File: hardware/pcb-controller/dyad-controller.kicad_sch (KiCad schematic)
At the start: 36 parts, among them J1 USB_C_Receptacle_USB2.0, J2 SWD, J6 HC-FPC-0.5-20P-FH20, J7 HC-FPC-0.5-20P-FH20, J8 HC-FPC-0.5-14P-FH20, SW1 SW_Push, U1 W25Q128JVS, U2 USBLC6-2SC6, U3 RP2040, U4 XC6206PxxxMR-Regulator_Linear, Y1 12MHz

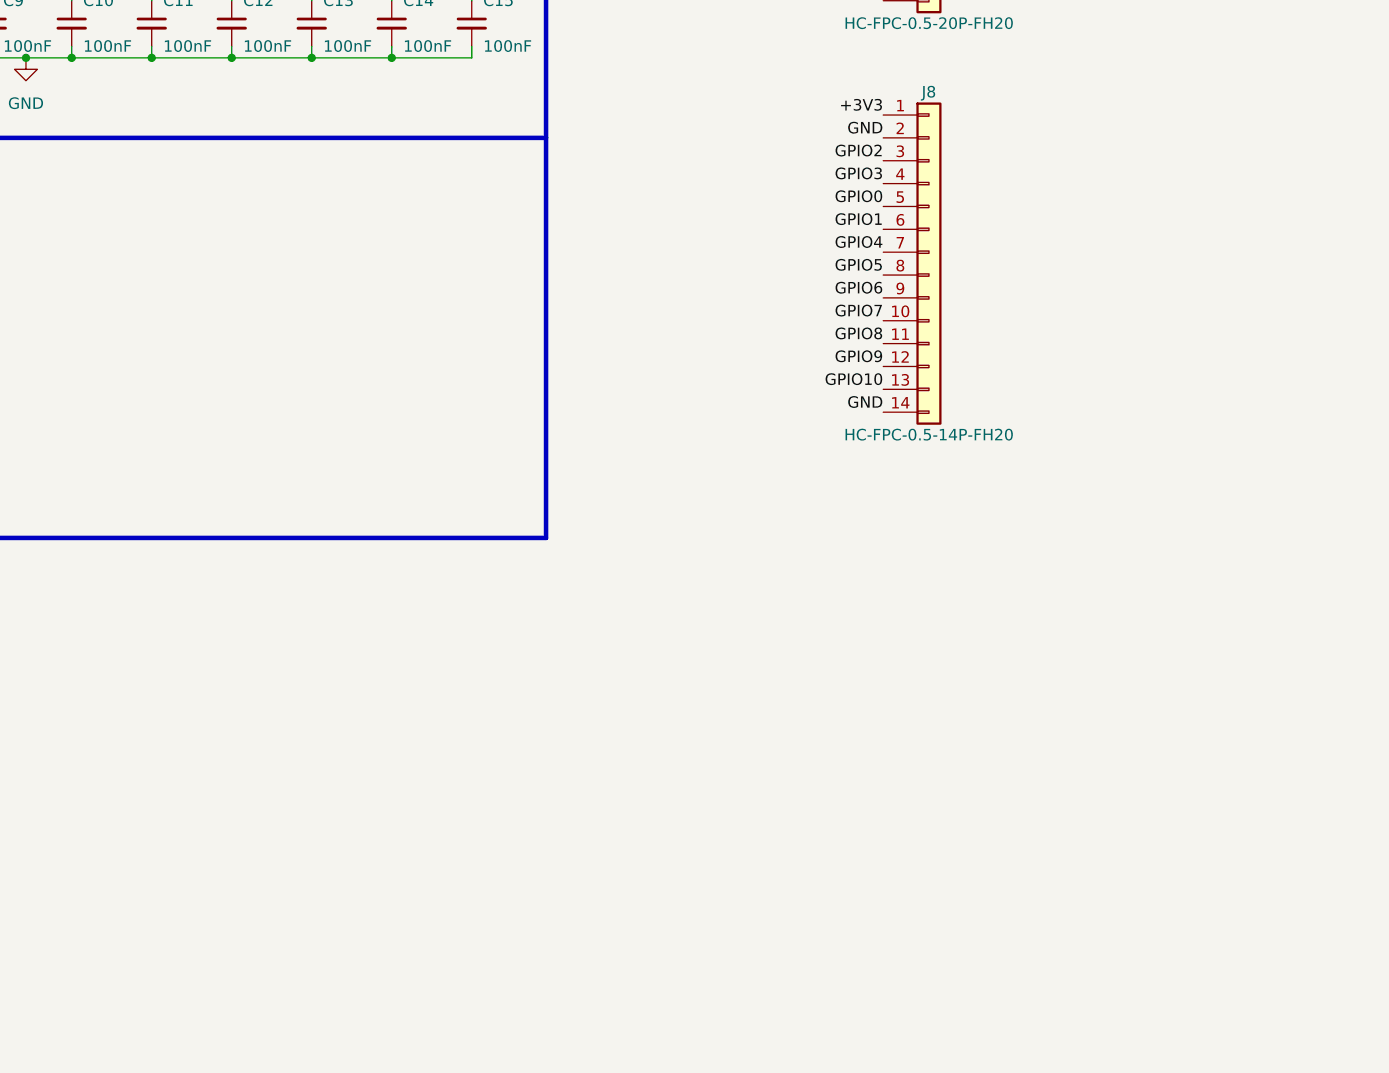
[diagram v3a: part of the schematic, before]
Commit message: Add the split-link USB-C, duplicated on both side edges
J9 and J10, same receptacle and footprint as the host J1 per PLAN.md §5,
one populated per half -- whichever faces the other half.

The host port stays a single footprint on the rear edge. The single
controller orientation the two-FFC decision buys means a rear-edge port
lands identically in both halves, so the host needs no duplicating. The
split port is duplicated for **usability, not geometry**: PLAN.md §5 warns
that "two identical USB-C ports per half invite the wrong cable.
Distinguish them by case position and labelling." Two ports side by side on
the rear are not distinguishable by position, and on the slave half there is
no host cable plugged in to compare against. On the inboard edge the split
port is structurally unmistakable -- the cable to the other half leaves from
the side facing it.

Wired to the three safety rules, not around them:

  CC1/CC2 no-connect (rule 1) -- a compliant source enables no VBUS without
  an Rd, so plugging the split port into a host is inert.
  SBU1 and SBU2 both tied to GPIO11 (rule 2) -- USB-C is reversible, and a
  single SBU pin would drop the link on a flipped plug.
  VBUS on its own VBUS_SPLIT rail (rule 3), awaiting its fuse and OR-ing
  Schottky, which are the next parts due.

D+/D- is deliberately left unconnected. The split link is not USB; wiring
the D pair would mean a C-to-C cable shorting the two halves' RP2040 USB
data lines with both device PHYs driving. Both D pairs carry explicit
no-connect flags, 12 in total across the two connectors.

Numbers: errors 4 -> 3. GPIO11 clears -- it was the last of the fifteen the
header deletion exposed that a connector could fix. The remaining three are
GPIO27-29, the genuine spares. 0 shorts, 0 orphans, the same 4 overlaps
inherited from the vendored design.

The three lib_symbol_issues warnings are one pre-existing issue, not two new
ones: J1 has always carried "Symbol 'USB_C_Receptacle_USB2.0' not found in
library 'Conne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
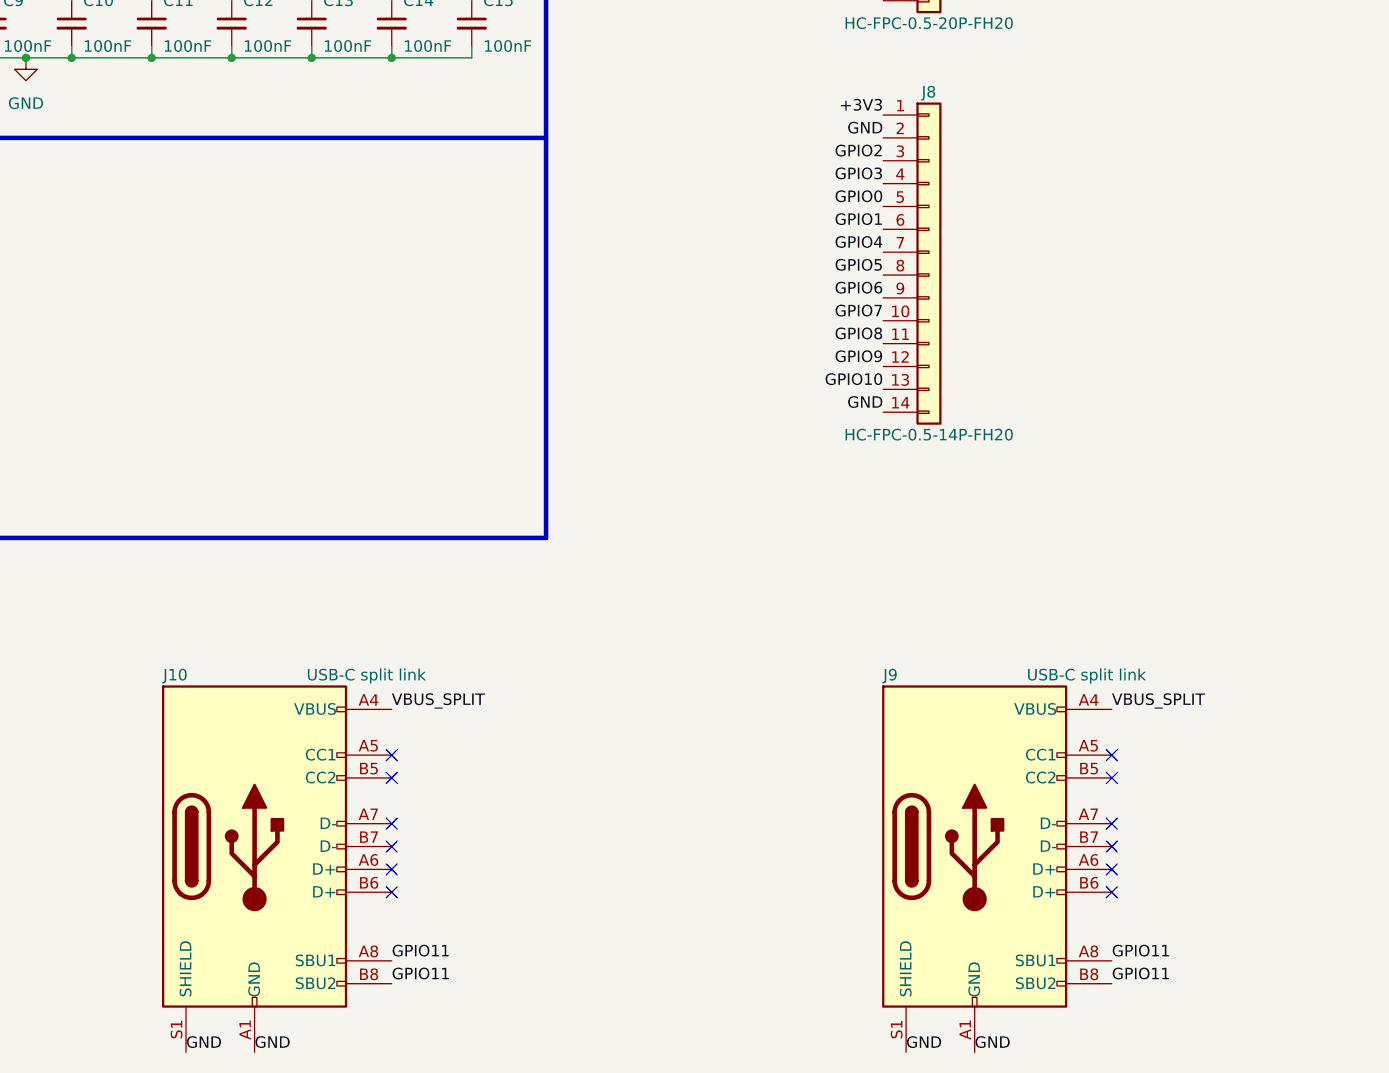
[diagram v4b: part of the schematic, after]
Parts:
- added J10, J9: USB-C split link, Connector_USB:USB_C_Receptacle_HRO_TYPE-C-31-M-12, symbol Connector:USB_C_Receptacle_USB2.0
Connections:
- net GND: now also J10.A1 (GND), J10.A12 (GND), J10.B1 (GND), J10.B12 (GND), J10.S1 (SHIELD), J9.A1 (GND), J9.A12 (GND), J9.B1 (GND), J9.B12 (GND), J9.S1 (SHIELD)
- net GPIO11: now also J10.A8 (SBU1), J10.B8 (SBU2), J9.A8 (SBU1), J9.B8 (SBU2)
- new net VBUS_SPLIT: J10.A4 (VBUS), J10.A9 (VBUS), J10.B4 (VBUS), J10.B9 (VBUS), J9.A4 (VBUS), J9.A9 (VBUS), J9.B4 (VBUS), J9.B9 (VBUS)
- no-connect marks 2 -> 14

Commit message: Add the split-VBUS fuse and the 5 V OR-ing Schottky
F2 (500 mA polyfuse, C70076, same part as F1) on the split VBUS, and D1
(SS34 Schottky, C8678, JLCPCB Basic, 3 A / 40 V) in the host VBUS path.
This completes PLAN.md §5 rule 3.

  host VBUS --F1--> VBUS_FUSED -->|D1--+--> +5V  (LDO, ESD, LED rail)
                                        |
                    split VBUS --F2-----+       (J9/J10, to the other half)

**Where the Schottky goes is not free choice** -- it decides whether one
half can power the other. +5V is the shared node: it feeds this half and
reaches the other half through F2 and the cable, while each half's own VBUS
enters through its own D1, so two hosts can never meet VBUS-to-VBUS. That is
the hazard rule 3 actually names.

The alternatives fail. A diode on each input into +5V blocks cross-half
power entirely. A diode only on the split input is worse -- a half can
receive but none can ever send. The Schottky must sit in the host path.

This required surgery on the inherited power tree: F1 pin 2 fed +5V
directly, so the wire and its +5V symbol were removed and F1's output
renamed VBUS_FUSED, with D1 bridging to +5V. Verified by reading both nets
back -- VBUS_FUSED holds exactly F1 pin 2 and D1's anode, and +5V holds D1's
cathode, F2, the LDO input, the ESD part, C16, the PWR_FLAG and J6/J7.
Polarity confirmed from the symbol: D1 pin 2 is A, pin 1 is K.

**Consequence to price in: +5V is now ~4.6 V, not 5.0 V.** SS34 drops ~0.4 V
at 1 A. Downstream still has margin -- XC6206 needs ~3.55 V in, SK6812MINI-E
is specified from 3.7 V -- but PLAN.md §5's per-key RGB brightness budget
assumes a 5 V rail and should be re-checked against 4.6 V before the LED
ceiling is treated as final. Recorded in CONTROLLER.md §2 rather than left
to be discovered.

SS34 over the 1 A B5819W (C8598, also Basic) for headroom: with one port
feeding both halves the diode carries the whole board.

Numbers: errors unchanged at 3, still only GPIO27-29, the genuine spares.
endpoin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
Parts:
- added D1: SS34, Diode_SMD:D_SMA, symbol Device:D_Schottky
- added F2: 500mA, Fuse:Fuse_1206_3216Metric, symbol Device:Polyfuse_Small
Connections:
- net +5V: now also D1.1 (K), F2.2; no longer F1.2
- net VBUS_SPLIT: now also F2.1
- new net VBUS_FUSED: D1.2 (A), F1.2
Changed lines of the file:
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@@
 	(wire
 		(pts
-			(xy 272.415 29.21)
-			(xy 277.495 29.21)
-		)
-		(stroke
-			(width 0)
-			(type default)
-		)
-	)
-	(wire
-		(pts
 			(xy 93.98 107.95)
 			(xy 88.9 107.95)
@@
 		)
 	)
+  (label "VBUS_FUSED"
+    (at 272.415 29.21 0)
+    (fields_autoplaced yes)
+    (effects (font (size 1.27 1.27)) (justify left bottom))
+  )
+  (label "VBUS_FUSED"
+    (at 144.78 175.26 0)
+    (fields_autoplaced yes)
+    (effects (font (size 1.27 1.27)) (justify left bottom))
+  )
+  (label "+5V"
+    (at 137.16 175.26 180)
+    (fields_autoplaced yes)
+    (effects (font (size 1.27 1.27)) (justify right bottom))
+  )
+  (label "+5V"
+    (at 140.97 199.39 0)
+    (fields_autoplaced yes)
+    (effects (font (size 1.27 1.27)) (justify left bottom))
+  )
+  (label "VBUS_SPLIT"
+    (at 140.97 194.31 0)
+    (fields_autoplaced yes)
+    (effects (font (size 1.27 1.27)) (justify left bottom))
+  )
 	(symbol
 		(lib_id "Device:R_Small")
@@
 	)
 	(symbol
-		(lib_id "power:+5V")
-		(at 277.495 29.21 0)
-		(unit 1)
-		(exclude_from_sim no)
-		(in_bom yes)
-		(on_board yes)
-		(dnp no)
-		(fields_autoplaced)
-		(property "Reference" "#PWR09"
-			(at 277.495 33.02 0)
-			(hide yes)
-			(show_name no)
-			(do_not_autoplace no)
-			(effects
-				(font
-					(size 1.27 1.27)
-				)
-			)
-		)
-		(property "Value" "+5V"
-			(at 277.495 24.13 0)
-			(show_name no)
-			(do_not_autoplace no)
-			(effects
-				(font
-					(size 1.27 1.27)
-				)
-			)
-		)
-		(property "Footprint" ""
-			(at 277.495 29.21 0)
-			(hide yes)
-			(show_name no)
-			(do_not_autoplace no)
-			(effects
-				(font
-					(size 1.27 1.27)
-				)
-			)
-		)
-		(property "Datasheet" ""
-			(at 277.495 29.21 0)
-			(hide yes)
-			(show_name no)
-			(do_not_autoplace no)
-			(effects
-				(font
-					(size 1.27 1.27)
-				)
-			)
-		)
-		(property "Description" ""
-			(at 277.495 29.21 0)
-			(show_name no)
-			(do_not_autoplace no)
-			(effects
-				(font
-					(size 1.27 1.27)
-				)
-			)
-		)
-		(body_style 1)
-		(in_pos_files yes)
-		(pin "1"
-		)
-		(instances
-			(project "dyad-controller"
-				(path "/ba62e47e-9e07-4e97-ab08-24b670d50f97"
-					(reference "#PWR09")
-					(unit 1)
-				)
-			)
-		)
-	)
-	(symbol
 		(lib_id "power:GND")
 		(at 224.79 92.71 0)
@@
 			)
 		)
-		(instances
-			(project "dyad-controller"
-				(path "/ba62e47e-9e07-4e97-ab08-24b670d50f97"
-					(reference "J9")
-					(unit 1)
-				)
-			)
-		)
 		(property "Serves" "Split link, RIGHT-edge placement - populated on the LEFT half (faces the other half). CC unconnected per PLAN.md §5 rule 1; SBU1+SBU2 tied per rule 2; VBUS_SPLIT needs its fuse + OR-ing Schottky per rule 3."
 			(at 330.2 180.34 0)
@@
 				)
 			)
-		))
+		)
+		(instances
+			(project "dyad-controller"
+				(path "/ba62e47e-9e07-4e97-ab08-24b670d50f97"
+					(reference "J9")
+					(unit 1)
+				)
+			)
+		)
+	)
 	(symbol
 		(lib_id "Connector:USB_C_Receptacle_USB2.0")
@@
 			)
 		)
+		(property "Serves" "Split link, LEFT-edge placement - populated on the RIGHT half (faces the other half). CC unconnected per PLAN.md §5 rule 1; SBU1+SBU2 tied per rule 2; VBUS_SPLIT needs its fuse + OR-ing Schottky per rule 3."
+			(at 250.19 180.34 0)
+			(hide yes)
+			(effects
+				(font
+					(size 1.27 1.27)
+				)
+			)
+		)
 		(instances
 			(project "dyad-controller"
@@
 			)
 		)
-		(property "Serves" "Split link, LEFT-edge placement - populated on the RIGHT half (faces the other half). CC unconnected per PLAN.md §5 rule 1; SBU1+SBU2 tied per rule 2; VBUS_SPLIT needs its fuse + OR-ing Schottky per rule 3."
-			(at 250.19 180.34 0)
+	)
+	(symbol
+		(lib_id "Device:D_Schottky")
+		(at 140.97 175.26 0)
+		(unit 1)
+		(in_bom yes)
+		(on_board yes)
+		(dnp no)
+		(property "Reference" "D1"
+			(at 140.97 172.72 0)
+			(effects
+				(font
+					(size 1.27 1.27)
+				)
+			)
+		)
+		(property "Value" "SS34"
+			(at 140.97 177.8 0)
+			(effects
+				(font
+					(size 1.27 1.27)
+				)
+			)
+		)
+		(property "Footprint" "Diode_SMD:D_SMA"
+			(at 140.97 175.26 0)
+			(hide yes)
+			(effects
+				(font
+					(size 1.27 1.27)
+				)
+			)
+		)
+		(property "Datasheet" ""
+			(at 140.97 175.26 0)
+			(hide yes)
+			(effects
+				(font
+					(size 1.27 1.27)
+				)
+			)
+		)
+		(property "Description" "Schottky diode"
+			(at 140.97 175.26 0)
+			(hide yes)
+			(effects
+				(font
+					(size 1.27 1.27)
+				)
+			)
+		)
+		(instances
+			(project "dyad-controller"
+				(path "/ba62e47e-9e07-4e97-ab08-24b670d50f97"
+					(reference "D1")
+					(unit 1)
+				)
+			)
+		)
+		(property "LCSC" "C8678"
+			(at 140.97 175.26 0)
+			(hide yes)
+			(effects
+				(font
+					(size 1.27 1.27)
+				)
+			)
+		))
+	(symbol
+		(lib_id "Device:Polyfuse_Small")
+		(at 140.97 196.85 0)
+		(unit 1)
+		(in_bom yes)
+		(on_board yes)
+		(dnp no)
+		(property "Reference" "F2"
+			(at 139.065 196.85 90)
+			(effects
+				(font
+					(size 1.27 1.27)
+				)
+			)
+		)
+		(property "Value" "500mA"
+			(at 142.875 196.85 90)
+			(effects
+				(font
+					(size 1.27 1.27)
+				)
+			)
+		)
+		(property "Footprint" "Fuse:Fuse_1206_3216Metric"
+			(at 140.97 196.85 0)
+			(hide yes)
+			(effects
+				(font
+					(size 1.27 1.27)
+				)
+			)
+		)
+		(property "Datasheet" ""
+			(at 140.97 196.85 0)
+			(hide yes)
+			(effects
+				(font
+					(size 1.27 1.27)
+				)
+			)
+		)
+		(property "Description" "Resettable fuse, polymeric positive temperature coefficient, small symbol"
+			(at 140.97 196.85 0)
+			(hide yes)
+			(effects
+				(font
+					(size 1.27 1.27)
+				)
+			)
+		)
+		(instances
+			(project "dyad-controller"
+				(path "/ba62e47e-9e07-4e97-ab08-24b670d50f97"
+					(reference "F2")
+					(unit 1)
+				)
+			)
+		)
+		(property "LCSC" "C70076"
+			(at 140.97 196.85 0)
 			(hide yes)
 			(effects
